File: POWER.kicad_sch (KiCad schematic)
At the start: 44 parts, among them SW1 SW_MEC_5E, U1 RT6222D, U3 RT4812, U6 RT5750A, U7 RT5750A, U8 RT6154A

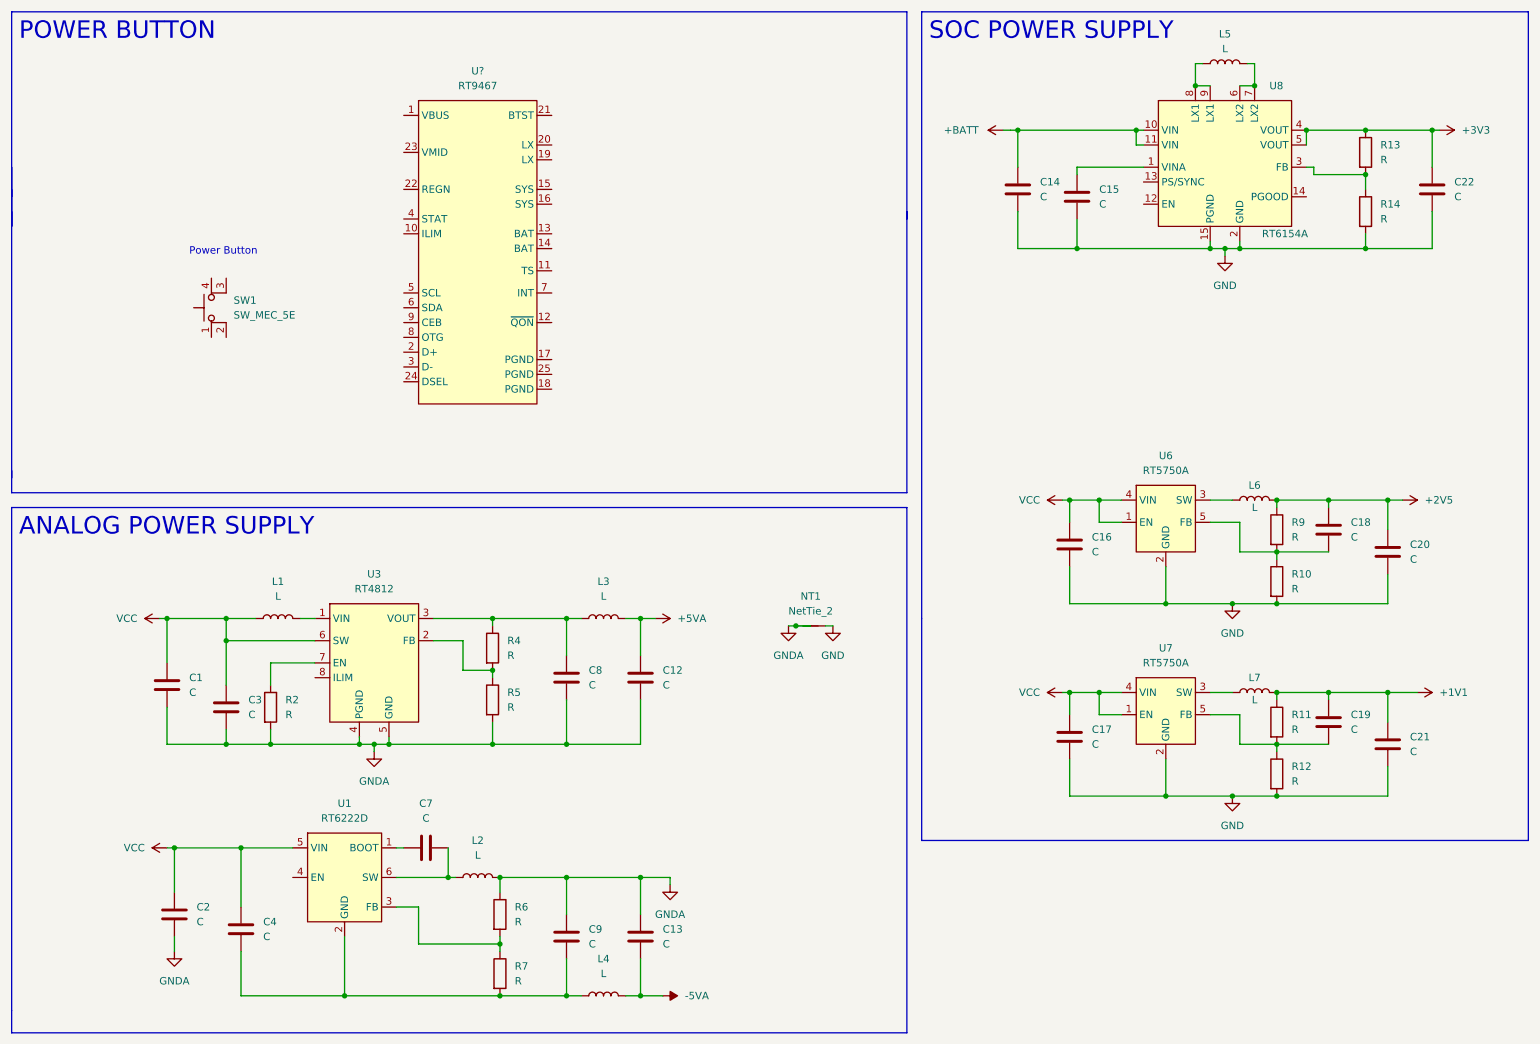
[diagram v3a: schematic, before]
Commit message: changer inverted buck ic
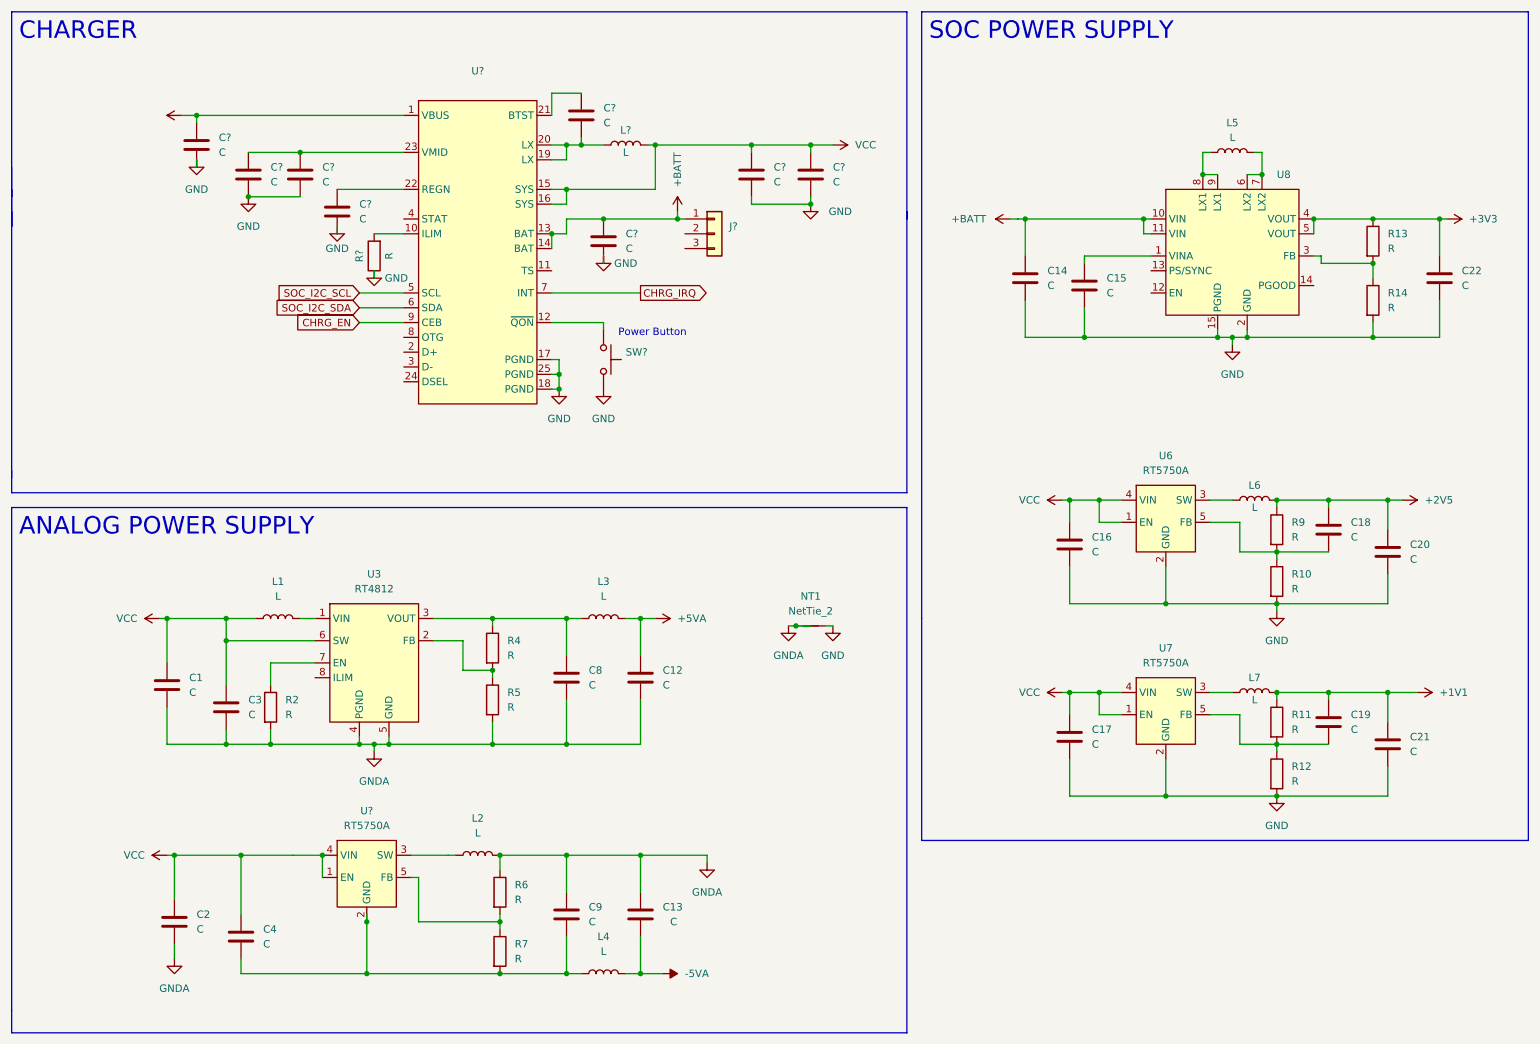
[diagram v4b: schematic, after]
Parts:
- removed C7: C, symbol rlib_passive:C
- removed SW1: SW_MEC_5E, symbol Switch:SW_MEC_5E
- removed U1: RT6222D, Package_TO_SOT_SMD:TSOT-23-6, symbol rlib_power:RT6222D
- added C? (x8): C, symbol rlib_passive:C
- added J?: (no value), symbol Connector_Generic:Conn_01x03
- added L?: L, symbol rlib_passive:L
- added R?: R, symbol rlib_passive:R
- added SW?: (no value), symbol rlib_buttons:KLS7-TS3606
- added U?: RT5750A, Package_TO_SOT_SMD:SOT-23-5, symbol rlib_power:RT5750A
- U8: value RT6154A -> (none)
- U?: value RT9467 -> (none); footprint Package_DFN_QFN:WQFN-24-1EP_4x4mm_P0.5mm_EP2.45x2.45mm -> (none)
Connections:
- net +BATT: now also U?.13 (BAT), U?.14 (BAT), C?.1, J?.1 (Pin_1)
- net GND: now also U?.17 (PGND), U?.18 (PGND), U?.25 (PGND), C?.2, C?.2, C?.2, C?.2, C?.2, C?.2, C?.2, R?.1, SW?.2
- net VCC: now also U?.15 (SYS), U?.16 (SYS), C?.1, C?.1, L?.2, U?.1 (EN), U?.4 (VIN)
- net at L2.1: now also U?.3 (SW)
- net at C4.2, C9.2, L4.1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: now also U?.2 (GND)
- net at R6.2, R7.1: now also U?.5 (FB)
- net VBUS: now reaches U?.1 (VBUS)
- net VBUS: now also C?.1
- net at U?.10 (ILIM): now also R?.2
- net at U?.12 (~{QON}): now also SW?.1
- net at U?.19 (LX): now also U?.20 (LX), C?.2, L?.1
- net at U?.21 (BTST): now also C?.1
- net at U?.22 (REGN): now also C?.1
- net at U?.23 (VMID): now also C?.1, C?.1
- net SOC_I2C_SCL: now reaches U?.5 (SCL)
- net SOC_I2C_SDA: now reaches U?.6 (SDA)
- net CHRG_IRQ: now reaches U?.7 (INT)
- net CHRG_EN: now reaches U?.9 (CEB)
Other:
- note added: "CHARGER"
- note removed: "POWER BUTTON"
- moved on the sheet: C13, C14, C15, C2, C22, C4, C9, L2, L4, L5, R13, R14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

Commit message: added winstar lcd
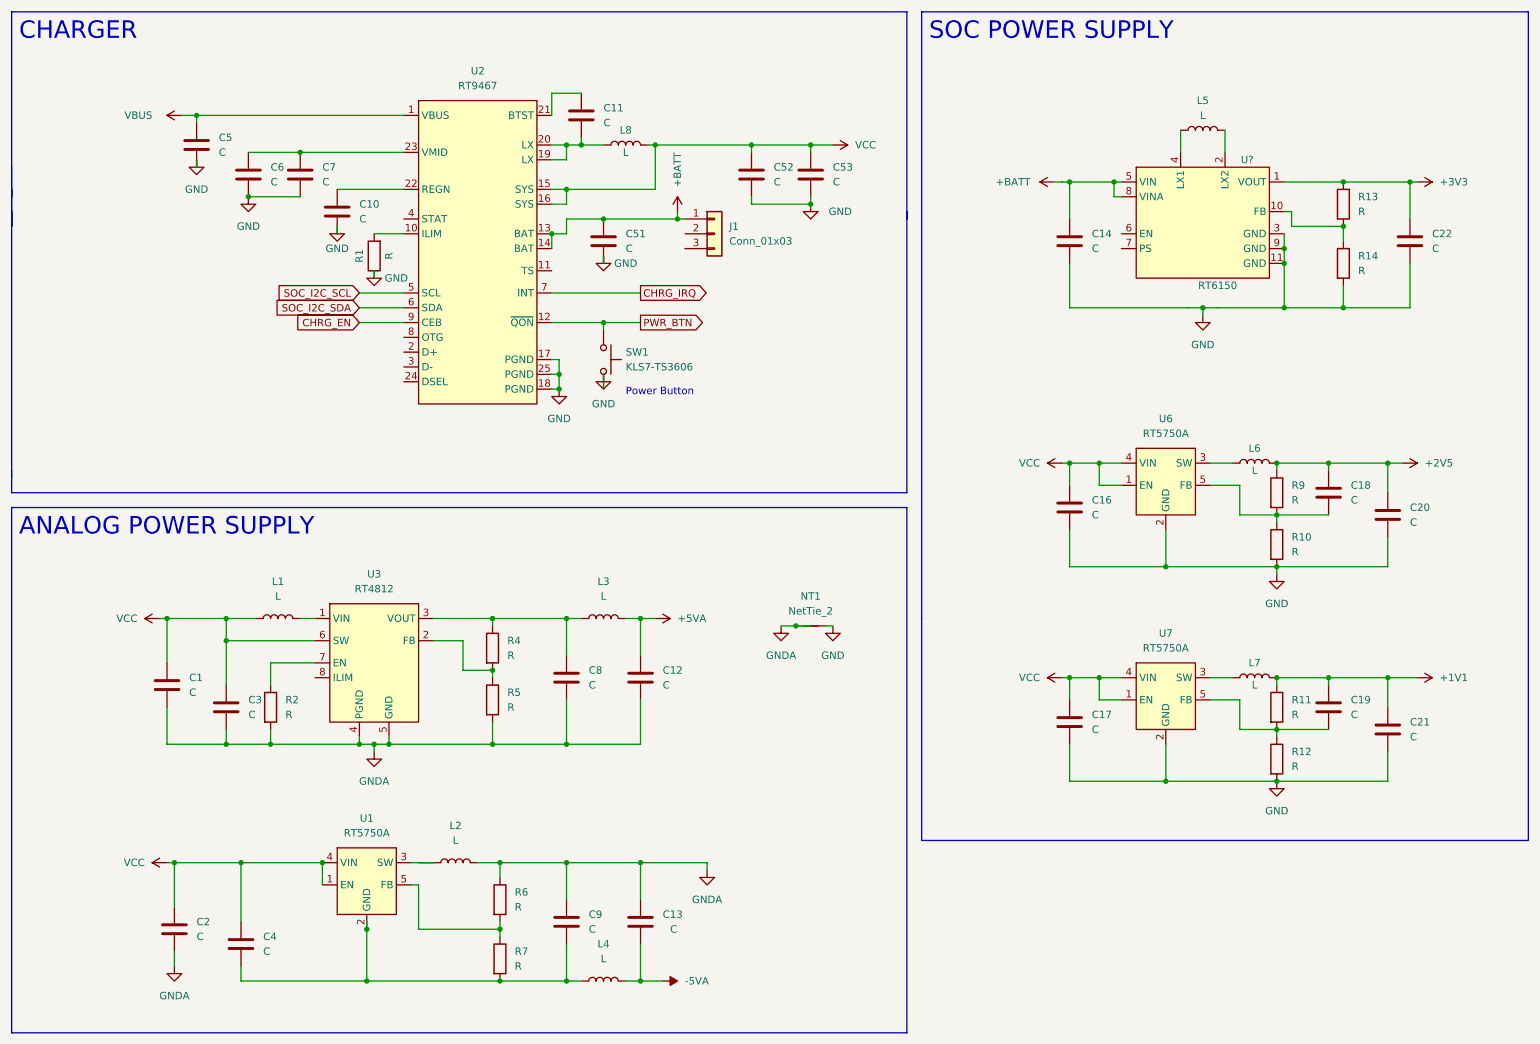
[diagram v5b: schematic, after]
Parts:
- removed C15: C, symbol rlib_passive:C
- removed U8: (no value), symbol rlib_power:RT6154A
- added U?: RT6150, symbol rlib_power:RT6150
- J1: renamed from J?; value (none) -> Conn_01x03
- SW1: renamed from SW?; value (none) -> KLS7-TS3606
- U1: renamed from U?; footprint Package_TO_SOT_SMD:SOT-23-5 -> rlib_power:SOT-23-5; Manufacturer (none) -> Richtek
- U2: renamed from U?; value (none) -> RT9467; footprint (none) -> rlib_power:WQFN-24-1EP_4x4mm_P0.5mm_EP2.45x2.45mm
- U3: footprint Package_TO_SOT_SMD:TSOT-23-8 -> rlib_power:TSOT-23-8; Manufacturer (none) -> Richtek
- U6, U7: footprint Package_TO_SOT_SMD:SOT-23-5 -> rlib_power:SOT-23-5; Manufacturer (none) -> Richtek
- gave numbers to parts that had none: 10
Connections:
- net +3V3: now also U?.1 (VOUT)
- net +BATT: now also U?.5 (VIN), U?.8 (VINA)
- net GND: now also U?.11 (GND), U?.3 (GND), U?.9 (GND)
- net PWR_BTN: now reaches SW1.1, U2.12 (~{QON})
- net at R13.2, R14.1: now also U?.10 (FB)
- net at L5.2: now also U?.2 (LX2)
- net at L5.1: now also U?.4 (LX1)
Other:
- moved on the sheet: C13, C14, C16, C17, C18, C19, C2, C20, C21, C22, C4, C9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

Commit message: added crystal,backlight regulator and usb nets
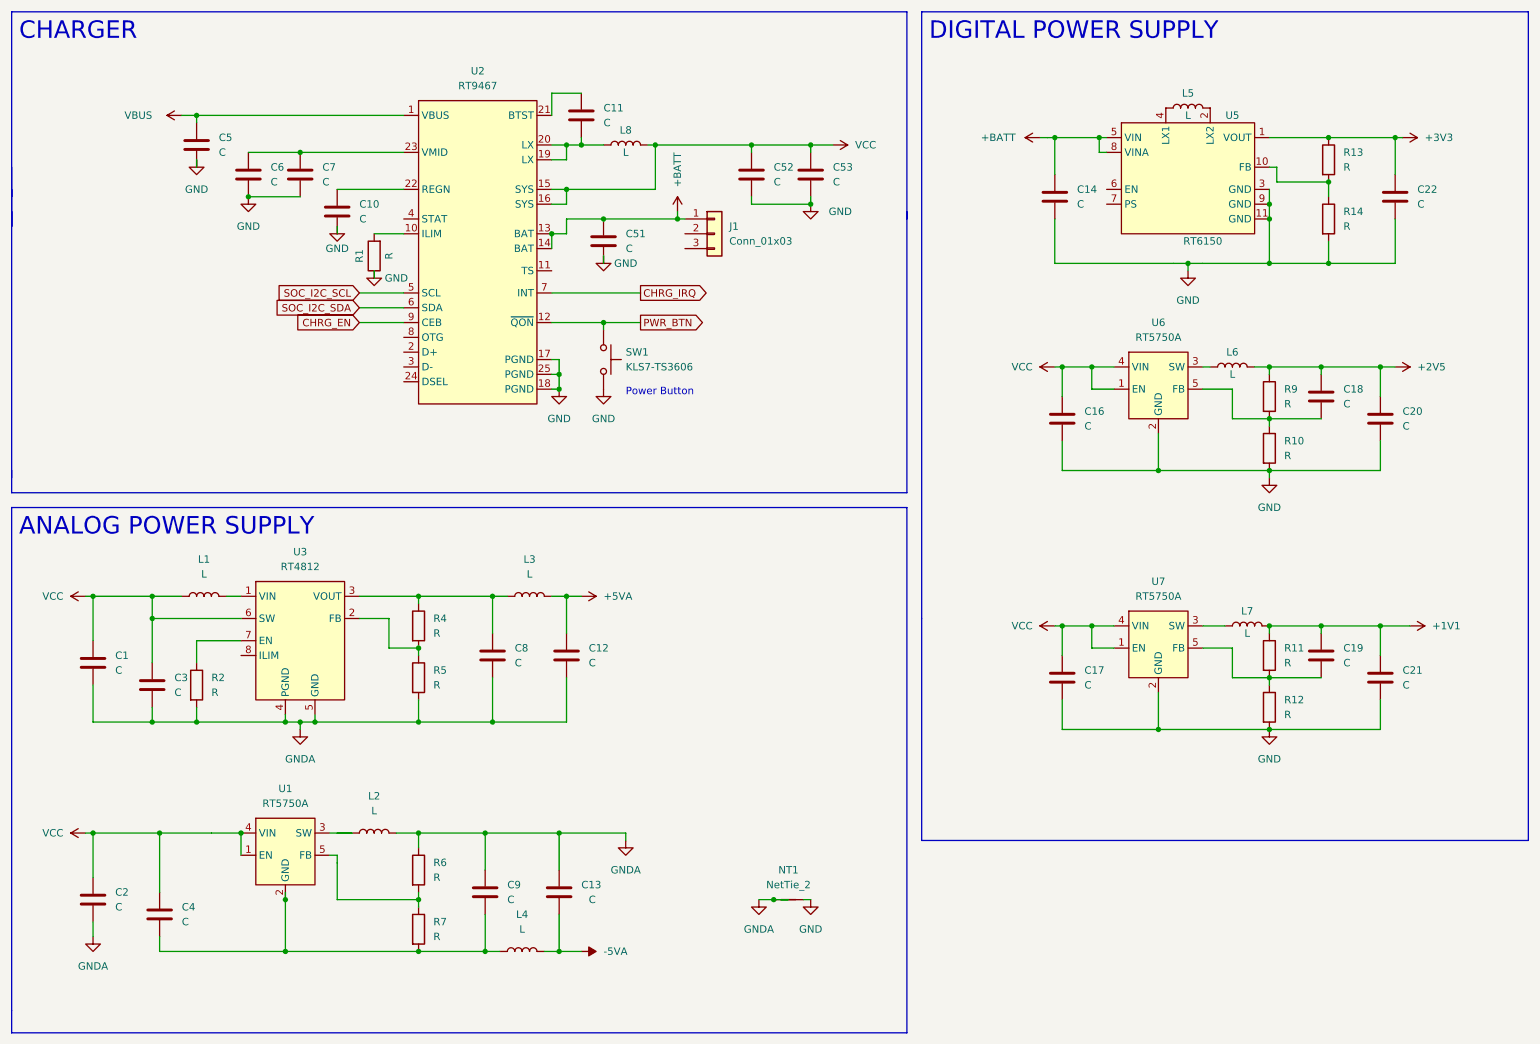
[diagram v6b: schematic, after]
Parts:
- U5: renamed from U?; footprint (none) -> rlib_power:RT6150AGQW
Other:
- note added: "DIGITAL POWER SUPPLY"
- note removed: "SOC POWER SUPPLY"
- moved on the sheet: C1, C12, C13, C14, C16, C17, C18, C19, C2, C20, C21, C22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

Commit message: changed volume buttons
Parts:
- SW1: footprint (none) -> rlib_buttons:TS-1010-X-X; symbol rlib_buttons:KLS7-TS3606 -> rlib_buttons:TS-1010-C-A
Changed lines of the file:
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@@
     (pin "1")
   )
-  (symbol (lib_id "rlib_buttons:KLS7-TS3606") (at 120.65 80.01 270) (unit 1)
+  (symbol (lib_id "rlib_buttons:TS-1010-C-A") (at 120.65 80.01 270) (unit 1)
     (in_bom yes) (on_board yes) (fields_autoplaced)
     (property "Reference" "SW1" (id 0) (at 124.46 78.7399 90)
@@
       (effects (font (size 1.27 1.27)) (justify left))
     )
-    (property "Footprint" "" (id 2) (at 125.73 80.01 0)
+    (property "Footprint" "rlib_buttons:TS-1010-X-X" (id 2) (at 115.57 78.74 0)
       (effects (font (size 1.27 1.27)) hide)
     )
-    (property "Datasheet" "${RLIB}/buttons/datasheets/KLS7-TS3606.pdf" (id 3) (at 125.73 80.01 0)
+    (property "Datasheet" "${RLIB}/buttons/datasheets/TS-1010-C-A.pdf" (id 3) (at 125.73 80.01 0)
       (effects (font (size 1.27 1.27)) hide)
     )

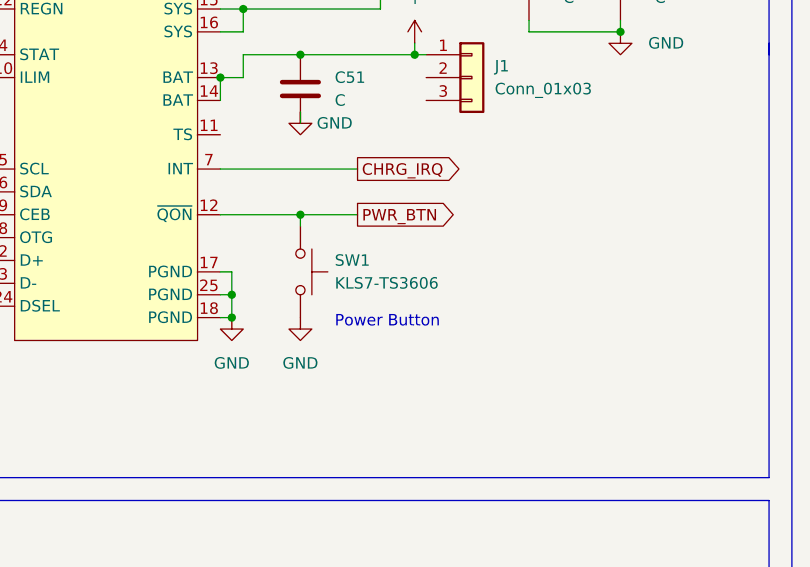
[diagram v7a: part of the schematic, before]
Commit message: added buttons
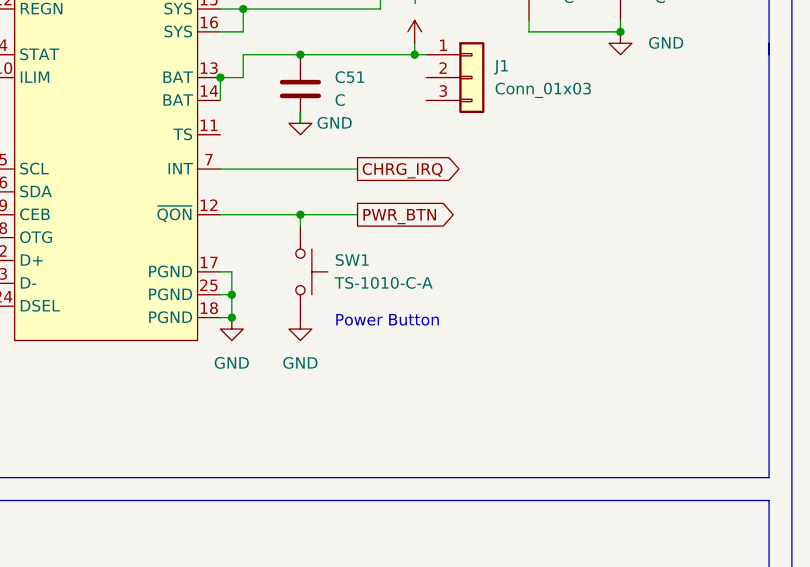
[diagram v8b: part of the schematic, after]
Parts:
- SW1: value KLS7-TS3606 -> TS-1010-C-A
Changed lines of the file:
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@@
       (effects (font (size 1.27 1.27)) (justify left))
     )
-    (property "Value" "KLS7-TS3606" (id 1) (at 124.46 81.2799 90)
+    (property "Value" "TS-1010-C-A" (id 1) (at 124.46 81.2799 90)
       (effects (font (size 1.27 1.27)) (justify left))
     )
@@
   )
   (symbol (lib_id "rlib_passive:R") (at 234.95 86.36 0) (unit 1)
-    (in_bom yes) (on_board yes) (fields_autoplaced)
+    (in_bom yes) (on_board yes)
     (property "Reference" "R9" (id 0) (at 237.49 85.0899 0)
       (effects (font (size 1.27 1.27)) (justify left))
